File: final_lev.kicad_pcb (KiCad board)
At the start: 2 copper layers, 181 parts, among them J101 +60V IN, J201 RAILS IN, J202 Conn_02x08_Odd_Even, J203 YOKE 1, J204 YOKE 2, Q1 IRF100B201, Q2 IRF100B201, Q201 IRF100B201, Q202 IRF100B201, Q203 IRF100B201, Q204 IRF100B201, Q3 IRF100B201, Q4 IRF100B201, U1 IR2184, U2 IR2184, U201 74LVC2G17, U202 74LVC2G17, U203 INA240A2D, U204 LM2903B, U205 74HCT74, U206 IR2184, U207 IR2184, U208 74HCT00, U3 INA240A2D, U4 LM2903B, U5 74HCT74, U6 74HCT00

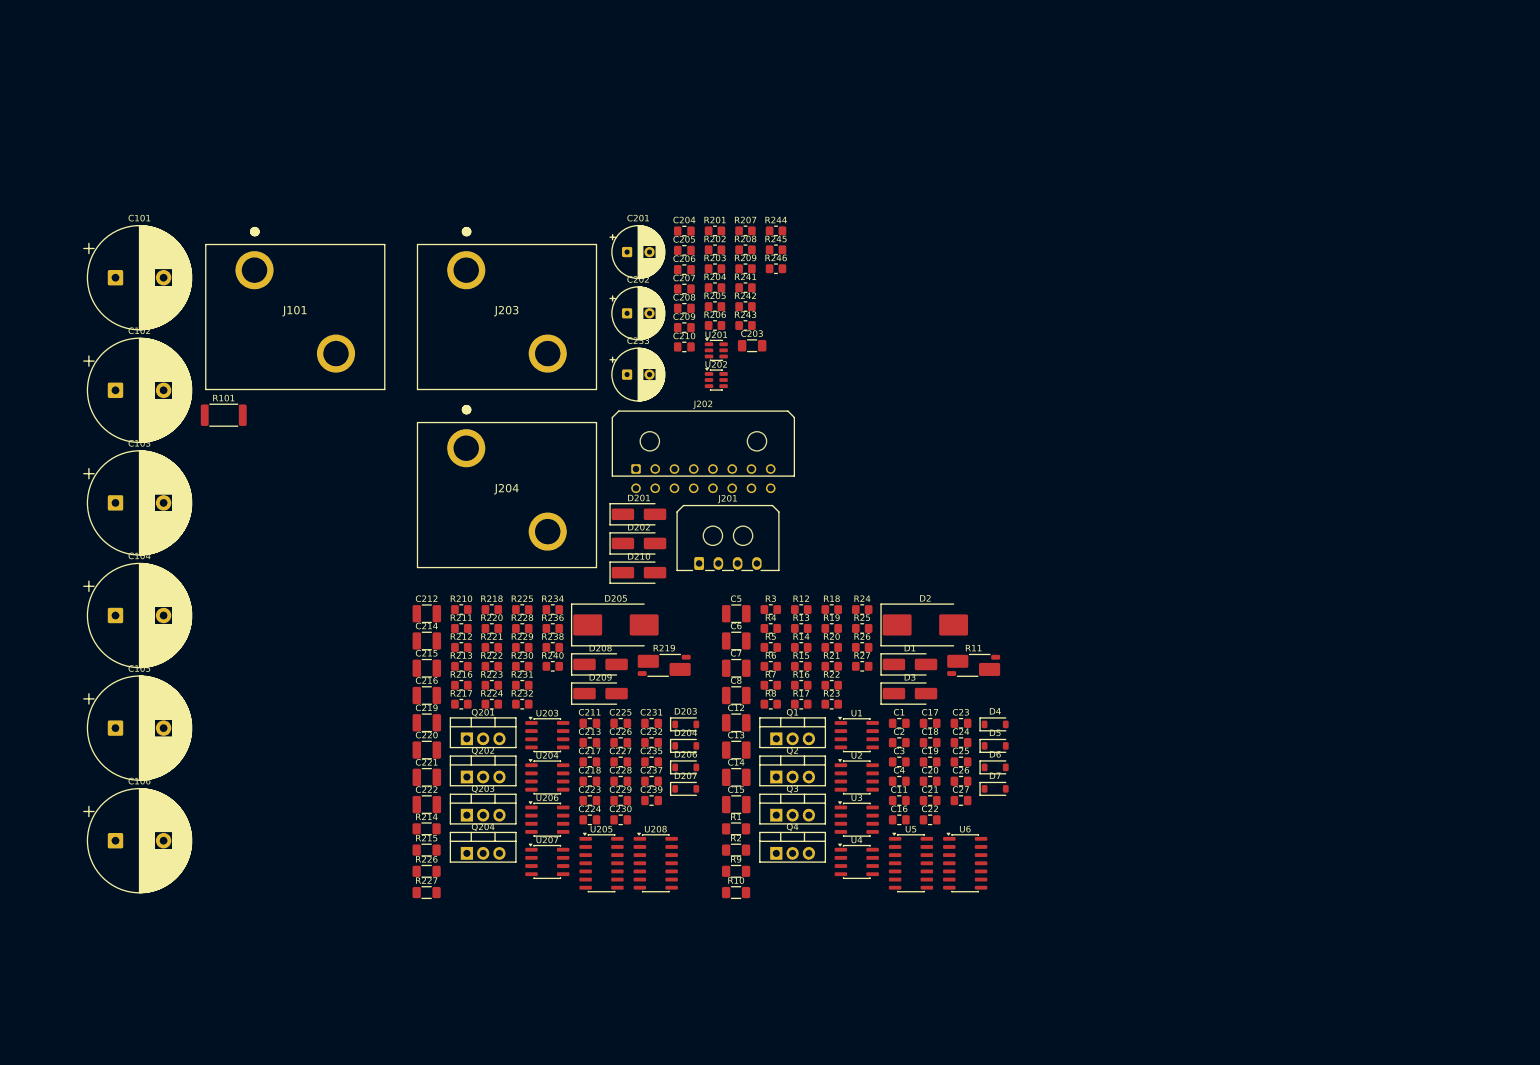
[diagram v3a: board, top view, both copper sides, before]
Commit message: Delta review fixes: POR timing, comparator supply, trip point, SD divider, Schmitt gate
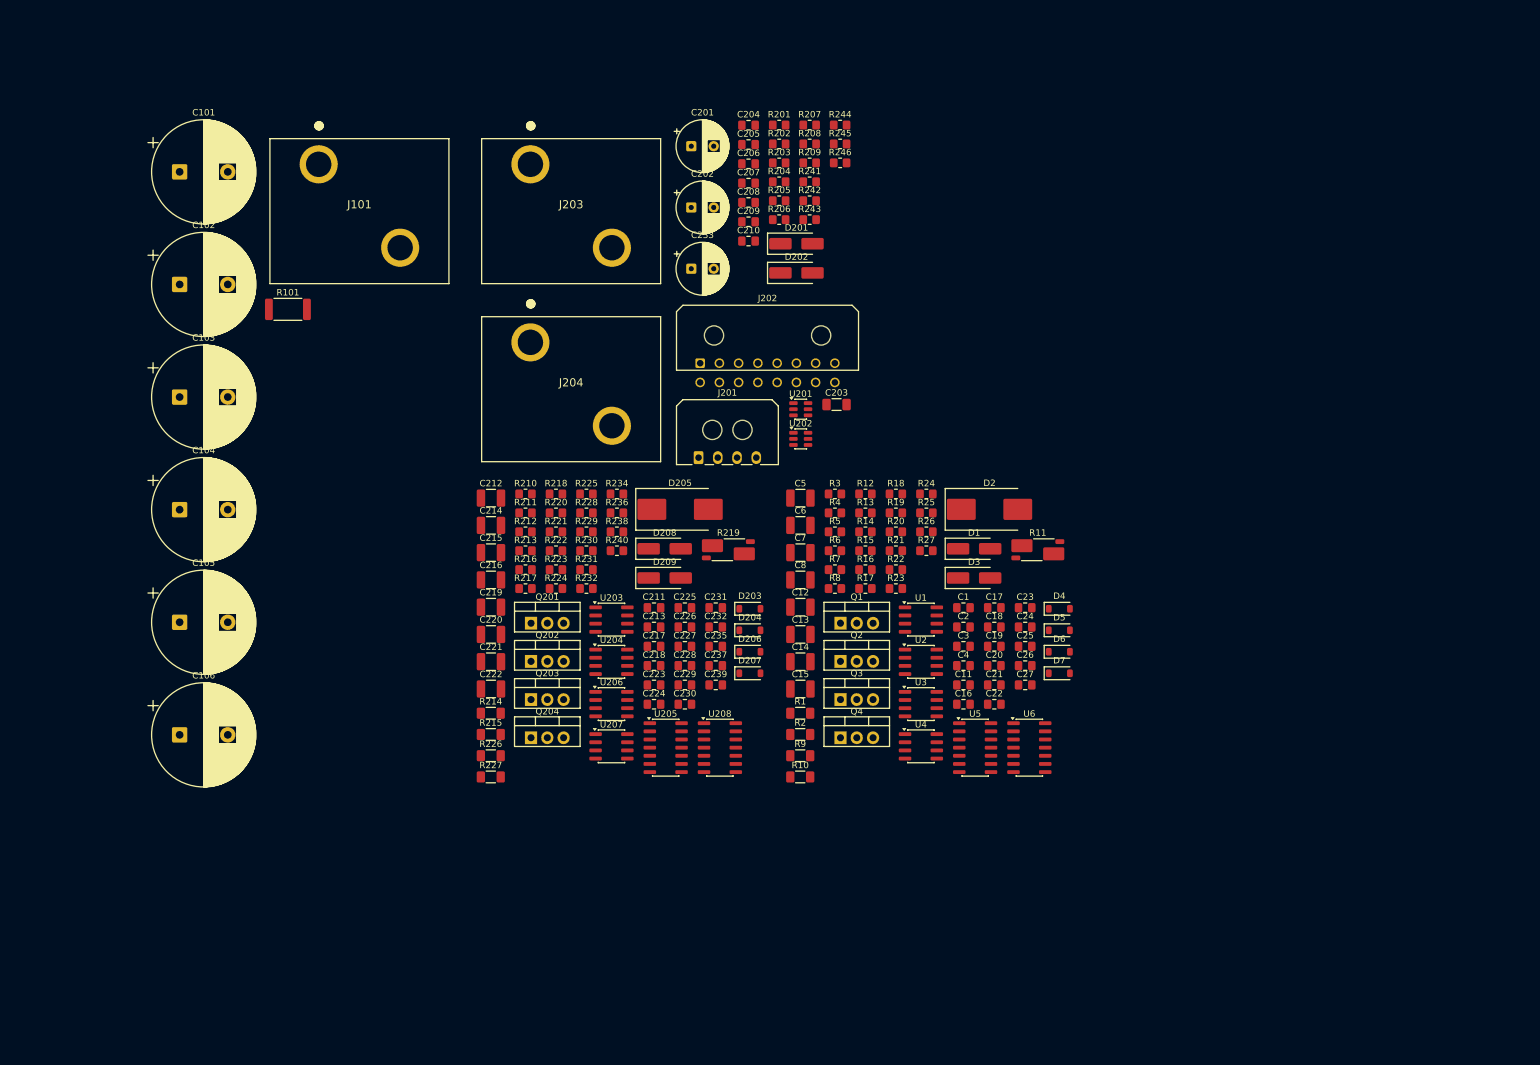
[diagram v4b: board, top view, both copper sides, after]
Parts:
- removed D210: SS34, Diode_SMD:D_SMA_Handsoldering
- C22, C224: value 100nF -> 1uF
- J202: value Conn_02x08_Odd_Even -> CONTROL
- R19, R230: value 10k -> 3.3k
- R234, R26: value 3.3k -> 1k
- U208, U6: value 74HCT00 -> 74HCT132
- moved D201 48.8 mm to (146.1, 64.0)
- moved D202 48.8 mm to (146.1, 68.5)
- moved C12 20.6 mm to (146.8, 120.6)
- moved C13 20.6 mm to (146.8, 124.9)
- moved C14 20.6 mm to (146.8, 129.1)
- moved C15 20.6 mm to (146.8, 133.4)
- moved C16 20.6 mm to (172.2, 135.8)
- moved C18 20.6 mm to (177.0, 123.7)
- moved C19 20.6 mm to (177.0, 126.7)
- moved C2 20.6 mm to (172.2, 123.7)
- moved C213 20.6 mm to (123.9, 123.7)
- moved C215 20.6 mm to (98.5, 112.1)
- moved C216 20.6 mm to (98.5, 116.4)
- moved C217 20.6 mm to (123.9, 126.7)
- moved C219 20.6 mm to (98.5, 120.6)
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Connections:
- C21 pad 2: +5V -> +12V
- C218 pad 2: +5V -> +12V
- J201 pad 3: /IO_PROTECT/+3V3_IN -> +3.3V
- U204 pad 8: +5V -> +12V
- U4 pad 8: +5V -> +12V

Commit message: Interleave 180->90 deg; U5 D pin to fail-safe; doc sweep for stale interleave refs
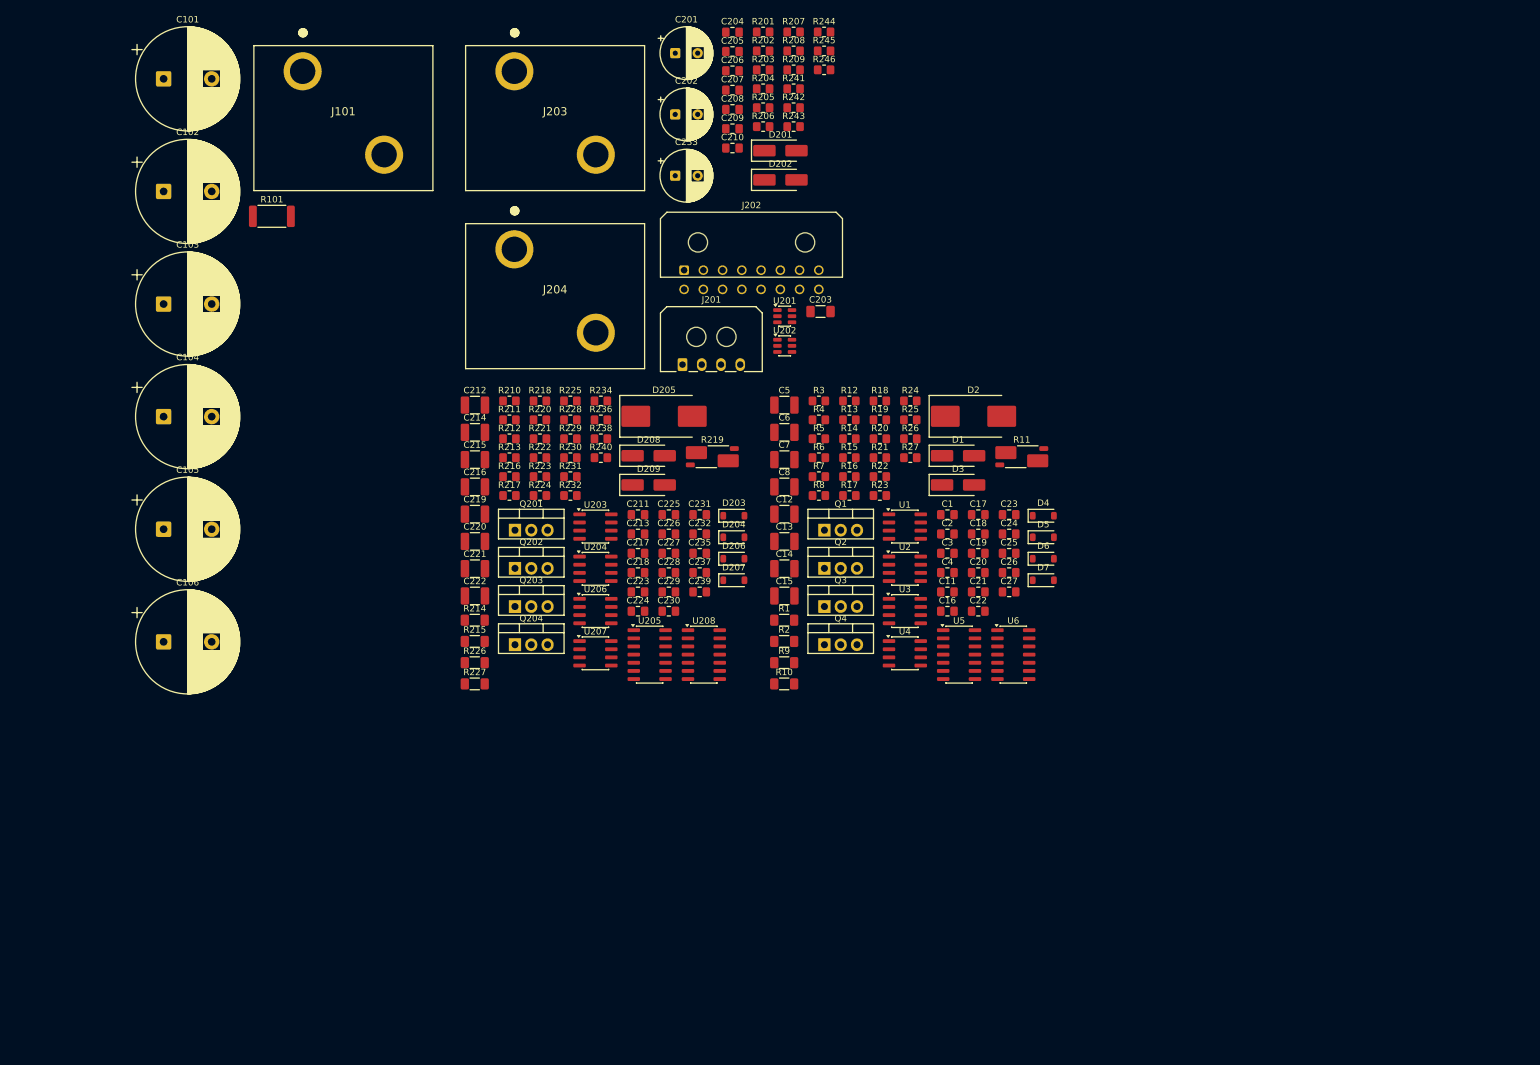
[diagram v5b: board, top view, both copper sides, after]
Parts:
- moved C20 14.7 mm to (174.5, 115.2)
- moved C218 14.7 mm to (121.4, 115.2)
- moved C228 14.7 mm to (126.2, 115.2)
- moved C237 14.7 mm to (131.1, 115.2)
- moved C26 14.7 mm to (179.3, 115.2)
- moved C4 14.7 mm to (169.7, 115.2)
- moved D207 14.7 mm to (136.4, 116.4)
- moved D7 14.7 mm to (184.6, 116.4)
- moved U2 14.7 mm to (163.0, 114.6)
- moved U204 14.7 mm to (114.8, 114.6)
- moved D202 14.7 mm to (143.6, 54.0)
- moved C204 14.7 mm to (136.2, 31.0)
- moved C1 14.7 mm to (169.7, 106.2)
- moved C101 14.7 mm to (47.5, 38.3)
- moved C102 14.7 mm to (47.5, 55.8)
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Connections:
- U205 pad 2: GND -> +5V
- U5 pad 2: GND -> +5V

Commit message: PCB placement complete (160x140, 184 fp, 0 courtyard overlaps); layout phase docs + lay.py; handoff
- Board resized 160x100 -> 160x140 after the courtyard-vs-pad-extent error
- Full placement of all 184 footprints, DRC clean except unconnected
- J203 moved inside the outline (x 107.0 -> 107.5), 0.450 mm margin
- docs/20_layout_phase.md: floorplan, verified metrics, CH2 leg-swap analysis
- docs/00_design_log.md: layout-phase entry incl. retraction of the
  'commutation loops trade values' claim (they are unchanged)
- tools/lay.py: courtyard-accurate layout checker, rescued from /tmp
- HANDOFF.md: remaining steps 1-3 with exact coordinates, transfer options

CH2 leg A/B swap analysed and verified but NOT applied.
2-layer vs 4-layer still undecided.
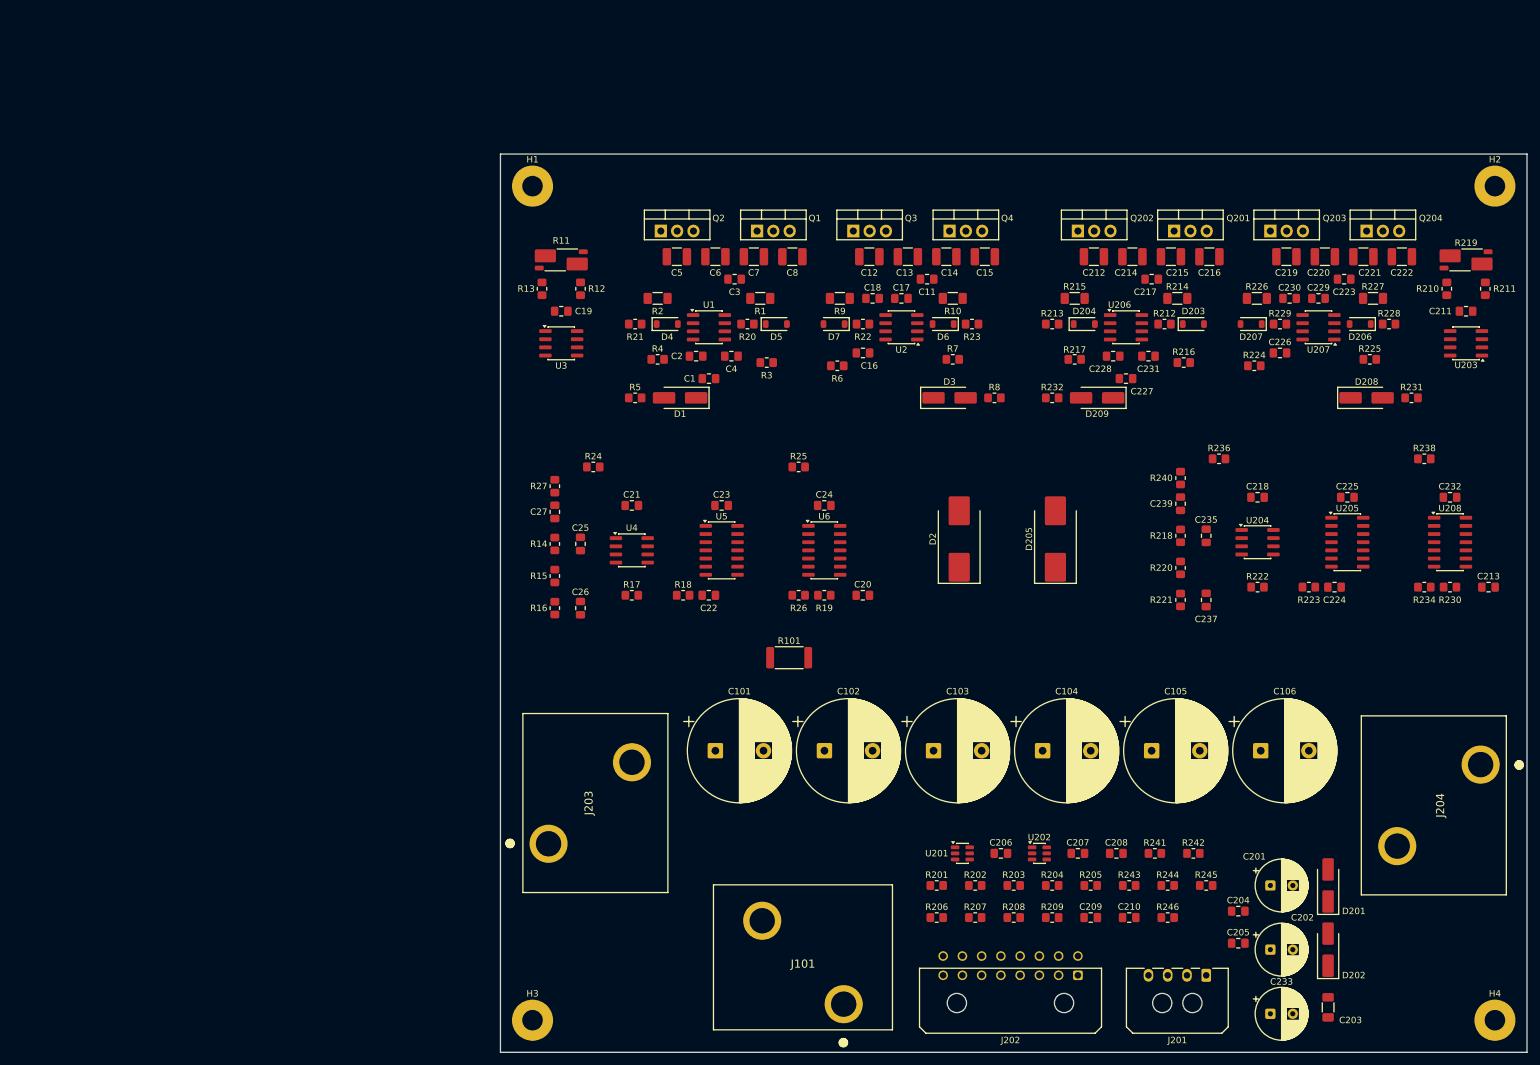
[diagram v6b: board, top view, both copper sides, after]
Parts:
- added H1: MountingHole, MountingHole:MountingHole_3.2mm_M3_Pad, F.Cu at (105.0, 55.0)
- added H2: MountingHole, MountingHole:MountingHole_3.2mm_M3_Pad, F.Cu at (255.0, 55.0)
- added H3: MountingHole, MountingHole:MountingHole_3.2mm_M3_Pad, F.Cu at (105.0, 185.0)
- added H4: MountingHole, MountingHole:MountingHole_3.2mm_M3_Pad, F.Cu at (255.0, 185.0)
- moved C106 171.8 mm to (218.5, 143.0)
- moved J204 170.7 mm to (252.8, 145.2), turned to -90 degrees
- moved J101 168.1 mm to (153.5, 182.5), turned to 180 degrees
- moved C233 160.2 mm to (220.0, 184.0)
- moved C202 159.8 mm to (220.0, 174.0)
- moved C205 159.8 mm to (215.0, 173.0)
- moved C201 159.5 mm to (220.0, 164.0)
- moved C204 158.1 mm to (215.0, 168.0)
- moved C105 157.8 mm to (201.5, 143.0)
- moved C222 153.8 mm to (240.5, 66.0)
- moved R211 153.5 mm to (253.5, 71.0), turned to 90 degrees
- moved R227 152.4 mm to (236.0, 72.5)
- moved Q204 147.6 mm to (235.0, 62.0)
- moved D202 147.2 mm to (229.0, 174.0), turned to 90 degrees
- moved R210 147.1 mm to (247.5, 71.0), turned to 90 degrees
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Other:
- board outline added: 160 x 140 mm

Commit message: CH2 leg A/B swap applied: SW_A 55.6 -> 25.8 mm
Leg B -30 mm X, leg A +30 mm X (42 footprints incl. bridge ceramics).
Y and rotation unchanged on every part.

Verified after the move:
  /CH2/SW_A      55.6 -> 25.8 mm
  /CH2/COIL_B2   97.0 -> 105.8 mm  (accepted cost)
  courtyard overlaps           0
  commutation loops unchanged  CH2 A 17.7 mm, CH2 B 16.7 mm
  FET thermal order            C-H-C-H preserved on both channels
  heatsink shadow              no intrusions
  all 42 coordinates exact against the target table

Applied by direct file patch after three Move Exactly dialogs landed on
wrong offsets (-32.08, -33.0, +29.5). KiCad closed for the patch; CRLF
line endings preserved (59557, unchanged); backup in _to_delete/.
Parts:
- moved C212 30.0 mm to (222.5, 66.0)
- moved C214 30.0 mm to (228.5, 66.0)
- moved C215 30.0 mm to (234.5, 66.0)
- moved C216 30.0 mm to (240.5, 66.0)
- moved C217 30.0 mm to (231.5, 69.5)
- moved C219 30.0 mm to (192.5, 66.0)
- moved C220 30.0 mm to (198.5, 66.0)
- moved C221 30.0 mm to (204.5, 66.0)
- moved C222 30.0 mm to (210.5, 66.0)
- moved C223 30.0 mm to (201.5, 69.5)
- moved C226 30.0 mm to (191.5, 81.0)
- moved C227 30.0 mm to (227.5, 85.0)
- moved C228 30.0 mm to (225.5, 81.5)
- moved C229 30.0 mm to (197.5, 72.5)
- moved C230 30.0 mm to (193.0, 72.5)
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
